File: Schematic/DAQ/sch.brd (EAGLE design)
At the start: 100 x 80 mm, 46 parts, among them IC1 MCP23S17SP, IC2 MCP23S17SP, IC3 MCP23S17SP, IC4 74LS165N, U1 ATMEGA328P-PU

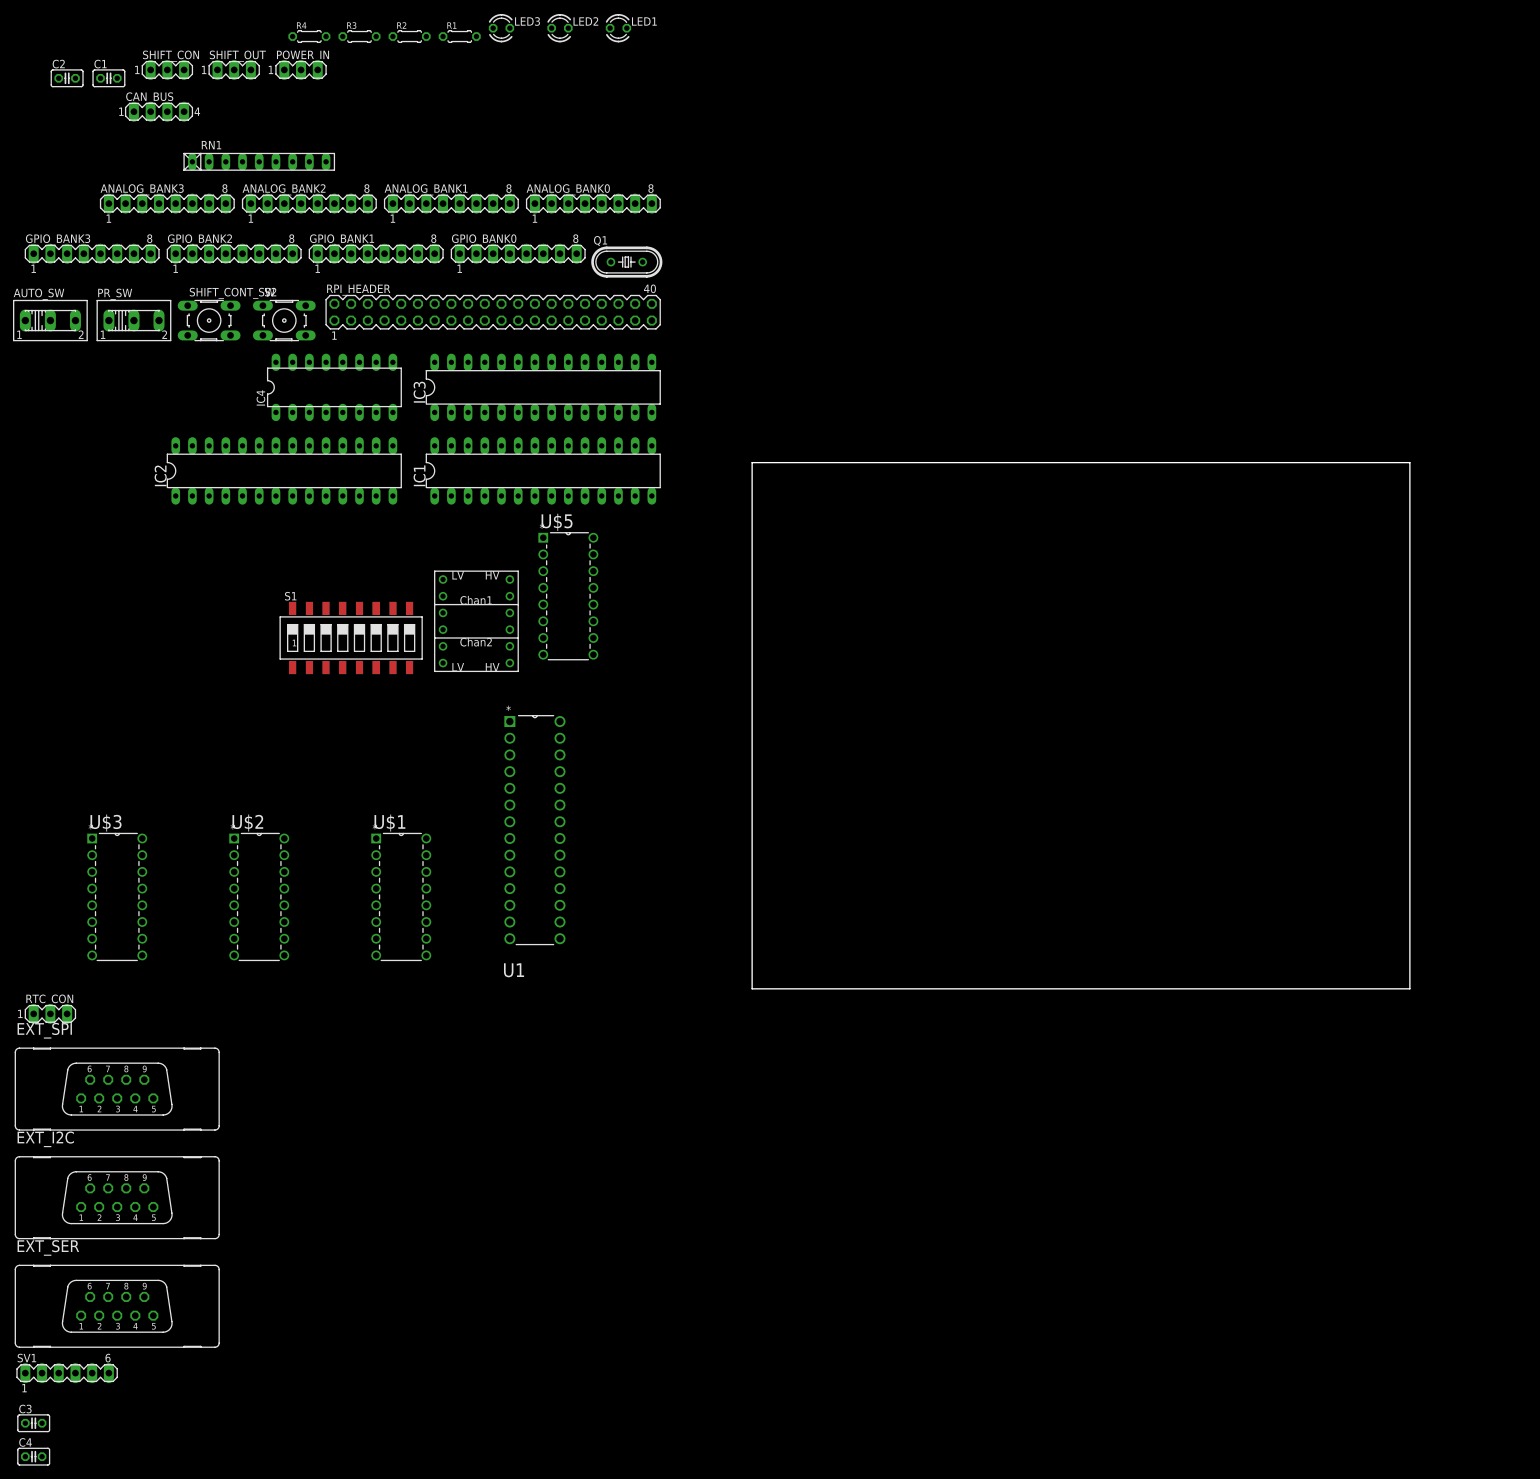
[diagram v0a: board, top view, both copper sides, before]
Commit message: basic board layout made
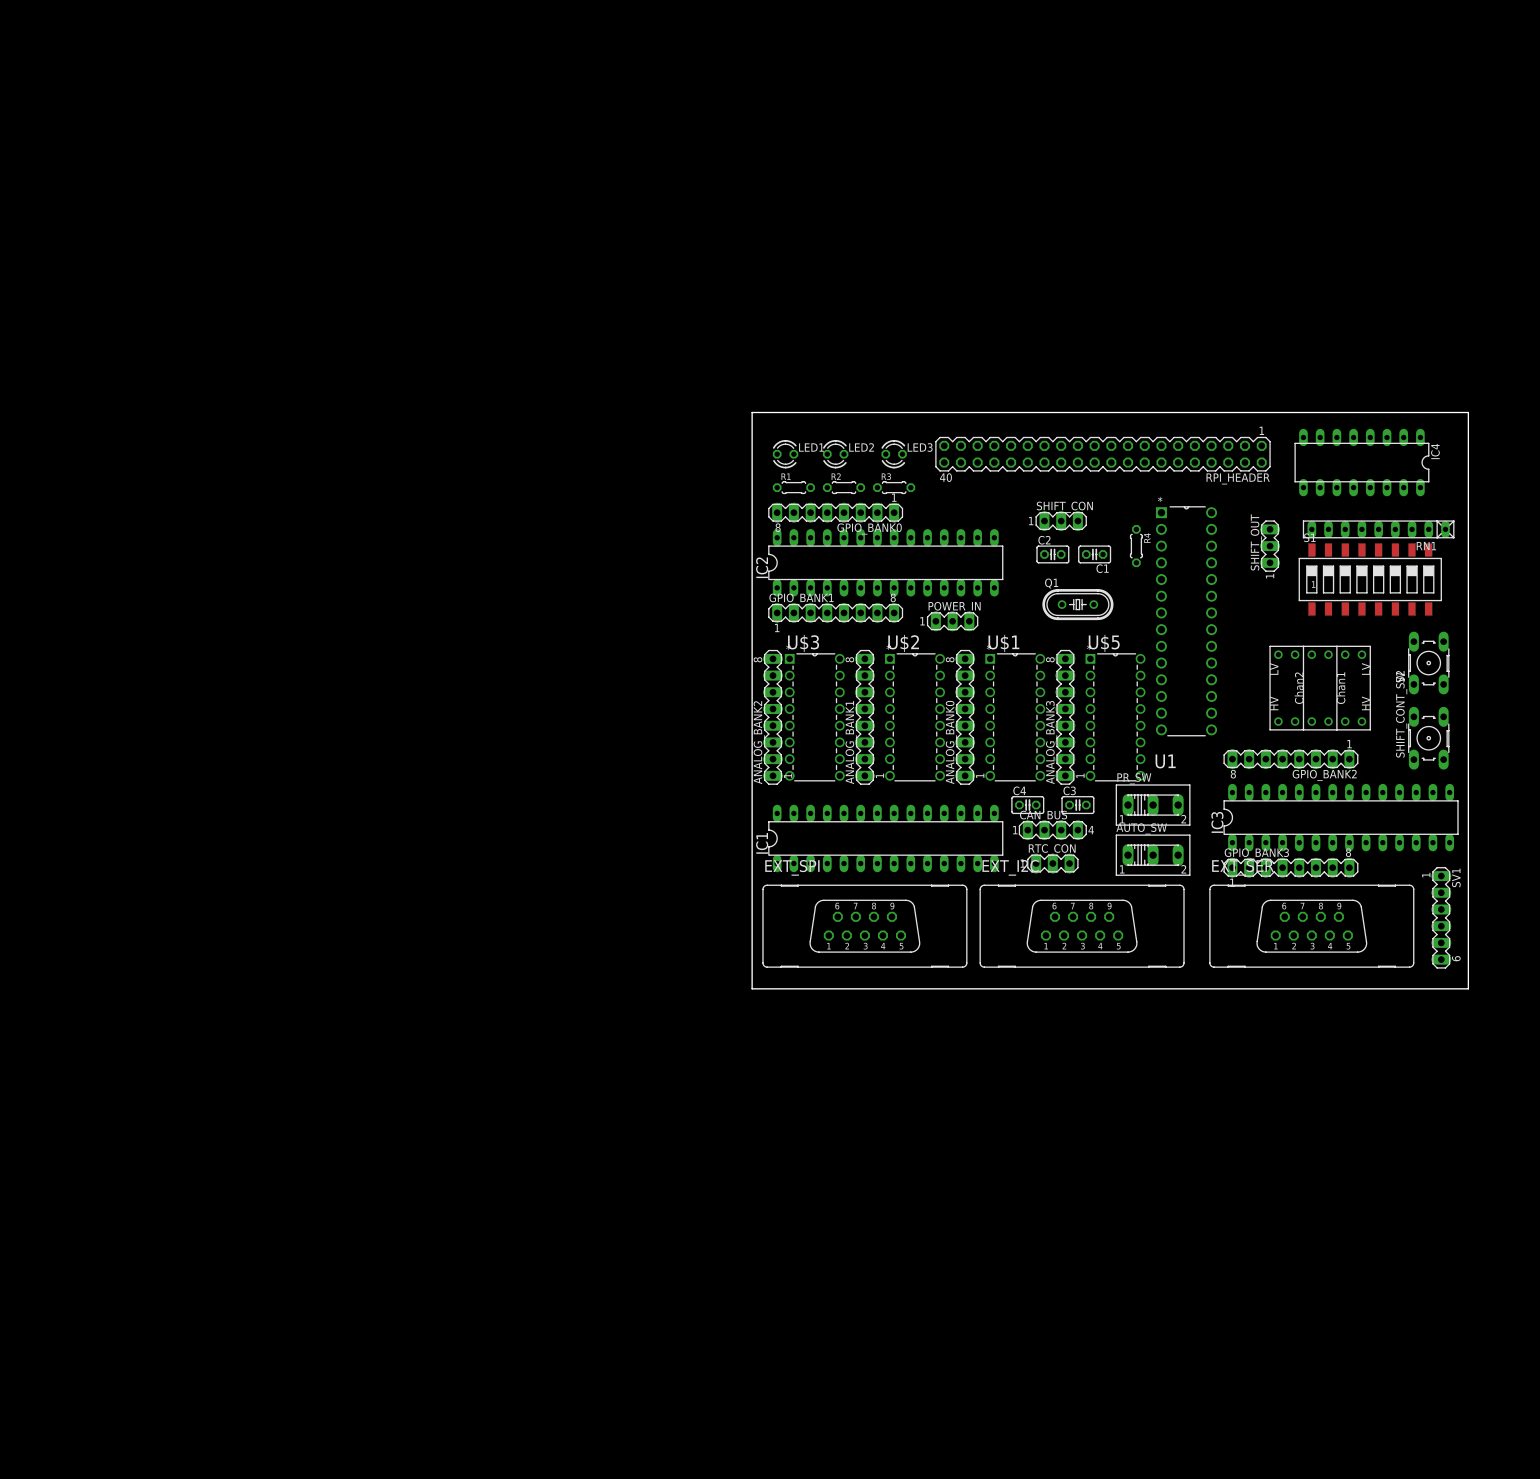
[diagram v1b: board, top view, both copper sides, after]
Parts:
- moved SV1 220.1 mm to (104.8, 10.8), turned to 270 degrees
- moved GPIO_BANK3 204.8 mm to (81.9, 18.4)
- moved SHIFT_CONT_SW 196.0 mm to (102.9, 38.1), turned to 90 degrees
- moved EXT_SER 190.6 mm to (85.1, 9.53)
- moved AUTO_SW 186.3 mm to (61.0, 20.3)
- moved C3 184.5 mm to (49.5, 27.9)
- moved S2 181.6 mm to (102.9, 49.5), turned to 90 degrees
- moved C4 180.7 mm to (41.9, 27.9)
- moved RN1 179.1 mm to (95.2, 69.8), turned to 180 degrees
- moved GPIO_BANK2 178.1 mm to (81.9, 34.9), turned to 180 degrees
- moved CAN_BUS 174.3 mm to (45.7, 24.1)
- moved SHIFT_OUT 173.3 mm to (78.7, 67.3), turned to 90 degrees
- moved PR_SW 171.6 mm to (61.0, 27.9)
- moved C1 166.4 mm to (52.1, 66.0), turned to 180 degrees
- moved C2 166.4 mm to (45.7, 66.0)
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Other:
- board size 100 x 80 mm -> 108.9 x 87.6 mm

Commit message: Started board
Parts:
- moved U$4 19.2 mm to (97.8, 54.6), turned to 180 degrees
- moved IC4 10.2 mm to (101.6, 85.1), turned to 0 degrees
- moved SHIFT_OUT 10.2 mm to (73.7, 76.2), turned to 180 degrees
- moved U1 9.67 mm to (78.7, 35.6)
- moved GPIO_BANK2 8.52 mm to (89.5, 31.1)
- moved IC3 8.03 mm to (97.2, 23.5)
- moved GPIO_BANK3 8.03 mm to (89.5, 15.9)
- moved LED2 7.73 mm to (14.0, 88.9)
- moved R2 7.73 mm to (15.2, 83.8)
- moved R3 7.73 mm to (22.9, 83.8)
- moved LED1 7.62 mm to (5.08, 88.9)
- moved LED3 7.62 mm to (21.6, 88.9)
- moved R1 7.62 mm to (6.35, 83.8)
- moved RPI_HEADER 6.48 mm to (54.6, 87.6)
- moved RN1 5.68 mm to (97.8, 74.9)
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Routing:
- net GND: track 0.00 -> 388.5 mm, vias 0 -> 1
- net 3V3: track 0.00 -> 154.1 mm, vias 0 -> 2
- net PR_RST: track 0.00 -> 114.9 mm, vias 0 -> 1
- net DAQ_SCK: track 0.00 -> 107.9 mm
- net DAQ_RX: track 0.00 -> 96.6 mm, vias 0 -> 1
- net DAQ_MISO: track 0.00 -> 78.6 mm, vias 0 -> 1
- net DAQ_MOSI: track 0.00 -> 77.2 mm
- net N$19: track 0.00 -> 73.6 mm, vias 0 -> 1
- net N$18: track 0.00 -> 72.7 mm, vias 0 -> 1
- net SH_OUT: track 0.00 -> 64.5 mm, vias 0 -> 3
- net N$32: track 0.00 -> 49.5 mm
- net N$31: track 0.00 -> 49.5 mm
- net N$30: track 0.00 -> 49.5 mm
- net GPIO_CS0: track 0.00 -> 49.0 mm
- net PR_VCC: track 0.00 -> 48.8 mm
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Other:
- board size 108.9 x 87.6 mm -> 121.6 x 99.1 mm

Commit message: DAQ Board Done
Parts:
- removed AUTO_SW: (no value), switch:255SB
- removed POWER_IN, SHIFT_CON, SHIFT_OUT: (no value), con-lstb:MA03-1
- added 5V_IN, 5V_IN1, 5V_IN2: (no value), con-lstb:MA03-1
- added EXT_SHIFT: (no value), con-subd:F09VB
- added SV2, SV3: (no value), con-lstb:MA04-1
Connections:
- removed net N$18: EXT_I2C.5, EXT_SER.5, EXT_SPI.5
- removed net N$19: EXT_I2C.1, EXT_SER.1, EXT_SPI.1
- new net N$59: EXT_SHIFT.8
- new net N$60: EXT_SHIFT.9
- net 3V3: now also EXT_I2C.1, EXT_SER.1, EXT_SHIFT.1, EXT_SPI.1
- net 5V: now also 5V_IN.1, 5V_IN.2, 5V_IN1.1, 5V_IN1.2, 5V_IN2.1, 5V_IN2.2; no longer POWER_IN.1, POWER_IN.2
- net GND: now also 5V_IN.3, 5V_IN1.3, 5V_IN2.3, EXT_I2C.5, EXT_SER.5, EXT_SHIFT.5, EXT_SPI.5; no longer AUTO_SW.3, POWER_IN.3
- net GPIO_12: now also SV2.4
- net GPIO_13: now also SV3.1
- net GPIO_16: now also SV3.2
- net GPIO_17: now also SV3.3
- net GPIO_20: now also SV3.4
- net GPIO_4: now also SV2.1
- net GPIO_5: now also SV2.2
- net GPIO_6: now also SV2.3
- net SDN_OUT: now also EXT_SHIFT.7; no longer SHIFT_OUT.3
- net SH_EN: now also EXT_SHIFT.4; no longer AUTO_SW.2
- net SH_SHDN: now also EXT_SHIFT.3; no longer SHIFT_CON.3
- net SH_SHUP: now also EXT_SHIFT.2; no longer SHIFT_CON.1
- net SH_VCC: no longer AUTO_SW.1
- net SU_OUT: now also EXT_SHIFT.6; no longer SHIFT_OUT.1
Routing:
- net N$19: track 73.6 -> 0.00 mm, vias 1 -> 0
- net N$18: track 72.7 -> 0.00 mm, vias 1 -> 0
- net GND: track 388.5 -> 442.8 mm, vias 1 -> 2
- net 5V: track 31.4 -> 23.8 mm
- net SU_OUT: track 11.2 -> 3.59 mm
- net SH_EN: track 28.0 -> 23.0 mm
- net SH_SHDN: track 29.8 -> 26.7 mm
- net SH_VCC: track 27.4 -> 25.5 mm
- net SH_SHUP: track 38.3 -> 37.7 mm

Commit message: DAQ board made
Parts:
- removed S1: SWS008, smd-special:SMS-008
- added SW1: (no value), SparkFun-Electromechanical:DIPSWITCH-08
- moved EXT_SHIFT 142.9 mm to (11.4, 123.2), turned to 90 degrees
- moved 5V_IN1 134.6 mm to (66.0, 68.6)
- moved SV3 132.9 mm to (80.0, 61.0)
- moved 5V_IN2 126.0 mm to (53.3, 61.0)
- moved SV2 119.3 mm to (66.0, 61.0), turned to 180 degrees
- moved 5V_IN 109.7 mm to (53.3, 81.3)
- moved SV1 107.8 mm to (34.3, 86.4), turned to 0 degrees
- moved C4 101.7 mm to (25.4, 128.3)
- moved C3 101.5 mm to (34.3, 128.3)
- moved PR_SW 101.4 mm to (86.4, 124.5), turned to 180 degrees
- moved ANALOG_BANK2 100.1 mm to (99.1, 12.7), turned to 180 degrees
- moved U$3 93.6 mm to (108.0, 25.4), turned to 90 degrees
- moved Q1 84.9 mm to (102.9, 124.5)
- moved EXT_SPI 83.6 mm to (11.4, 90.2), turned to 90 degrees
- moved ANALOG_BANK1 81.2 mm to (99.1, 31.8), turned to 180 degrees
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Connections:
- net 3V3: now also SW1.10, SW1.11, SW1.12, SW1.13, SW1.14, SW1.15, SW1.16, SW1.9; no longer S1.1, S1.2, S1.3, S1.4, S1.5, S1.6, S1.7, S1.8
- net N$10: now also SW1.8; no longer S1.16
- net N$11: now also SW1.7; no longer S1.15
- net N$12: now also SW1.6; no longer S1.14
- net N$13: now also SW1.5; no longer S1.13
- net N$14: now also SW1.4; no longer S1.12
- net N$15: now also SW1.3; no longer S1.11
- net N$16: now also SW1.2; no longer S1.10
- net N$17: now also SW1.1; no longer S1.9
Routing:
- net GND: track 442.8 -> 708.5 mm
- net 3V3: track 154.1 -> 406.9 mm, vias 2 -> 3
- net 5V: track 23.8 -> 229.1 mm
- net DAQ_MISO: track 78.6 -> 250.4 mm, vias 1 -> 2
- net DAQ_SYNC: track 0.00 -> 170.7 mm
- net DAQ_RX: track 96.6 -> 261.7 mm, vias 1 -> 3
- net XTAL2: track 8.72 -> 172.9 mm
- net N$4: track 0.00 -> 145.1 mm
- net N$36: track 0.00 -> 143.3 mm
- net SH_VCC: track 25.5 -> 156.3 mm, vias 0 -> 1
- net DAQ_TX: track 27.4 -> 151.6 mm, vias 0 -> 4
- net N$30: track 49.5 -> 164.0 mm, vias 0 -> 2
- net DAQ_MOSI: track 77.2 -> 185.8 mm, vias 0 -> 1
- net N$31: track 49.5 -> 152.3 mm, vias 0 -> 2
- net N$25: track 5.08 -> 105.8 mm, vias 0 -> 1
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- added copper zone on layer 1, net GND
- added copper zone on layer 16, net GND
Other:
- board size 121.6 x 99.1 mm -> 116.8 x 147 mm
- board text added: "Board: John Eng"
- board text added: "RFR 2015-2016"
- board text added: "Schematic: Samuel Stratter"

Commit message: DAQ Board done
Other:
- board size 116.8 x 147 mm -> 115.5 x 147 mm
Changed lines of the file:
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@@
 <board>
 <plain>
-<wire x1="0" y1="0" x2="116.82" y2="0" width="0" layer="20"/>
-<wire x1="116.82" y1="0" x2="116.82" y2="146.99" width="0" layer="20"/>
-<wire x1="116.82" y1="146.99" x2="0" y2="146.99" width="0" layer="20"/>
+<wire x1="0" y1="0" x2="115.55" y2="0" width="0" layer="20"/>
+<wire x1="115.55" y1="0" x2="115.55" y2="146.99" width="0" layer="20"/>
+<wire x1="115.55" y1="146.99" x2="0" y2="146.99" width="0" layer="20"/>
 <wire x1="0" y1="146.99" x2="0" y2="0" width="0" layer="20"/>
 <hole x="5.08" y="3.81" drill="0.6"/>
 <hole x="111.76" y="3.81" drill="0.6"/>
-<hole x="111.76" y="143.51" drill="0.6"/>
-<hole x="5.08" y="143.51" drill="0.6"/>
+<hole x="111.76" y="142.24" drill="0.6"/>
+<hole x="5.08" y="142.24" drill="0.6"/>
 <text x="66.04" y="139.7" size="2.1844" layer="21">Board: John Eng</text>
 <text x="66.04" y="135.89" size="2.1844" layer="21">Schematic: Samuel Stratter</text>

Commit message: Final Design Rev. 1
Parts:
- renumbered IC1 to CS_CONT, IC2 to GPIO_0, IC3 to GPIO_1, IC4 to SHIFT_IN, S2 to SHIFT_RST, SV1 to FTDI, SV2 to RPI_GPIO_0, SV3 to RPI_GPIO_1, SW1 to DIP_ARRAY, U$1 to ADC_0, U$2 to ADC_1, U$3 to ADC_2, U$4 to LOGIC_SHIFT, U$5 to ADC_3, U1 to SHIFT_CON
